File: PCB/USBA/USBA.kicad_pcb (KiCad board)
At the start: 2 copper layers, 70 x 70 mm, 23 parts, among them J1 USB_A, J2 Shelly, U2 ESP32-S3-MINI-1, U5 MD8942, U6 SHT40

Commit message: New reg
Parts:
- moved R10 1.30 mm to (104.8, 102.0), turned to 180 degrees
- moved R11 1.30 mm to (108.4, 102.0), turned to 180 degrees
- moved R1 0.30 mm to (108.7, 104.4)
- moved C3 0.30 mm to (108.7, 103.5)
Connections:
- U2 pad 21: unconnected-(U2-GPIO17-Pad21) -> GND
- U2 pad 22: unconnected-(U2-GPIO18-Pad22) -> GND
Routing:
- net GND: track 7.65 -> 7.76 mm, vias 15 -> 16

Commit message: Tidy
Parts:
- moved R4 0.10 mm to (104.8, 103.8)
- moved R5 0.10 mm to (104.8, 104.7)
- moved R7 0.10 mm to (104.8, 102.9)
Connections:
- U2 pad 21: GND -> unconnected-(U2-GPIO17-Pad21)
- U2 pad 22: GND -> unconnected-(U2-GPIO18-Pad22)
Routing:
- net GND: vias 16 -> 19

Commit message: Tweak
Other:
- board text added: "This PCB must be 1.2mm thick Please query if ordered otherwise"
- board text added: "This PCB must be 70x70mm Please query if ordered otherwise"
- board text removed: "Use 1.2mm PCB"

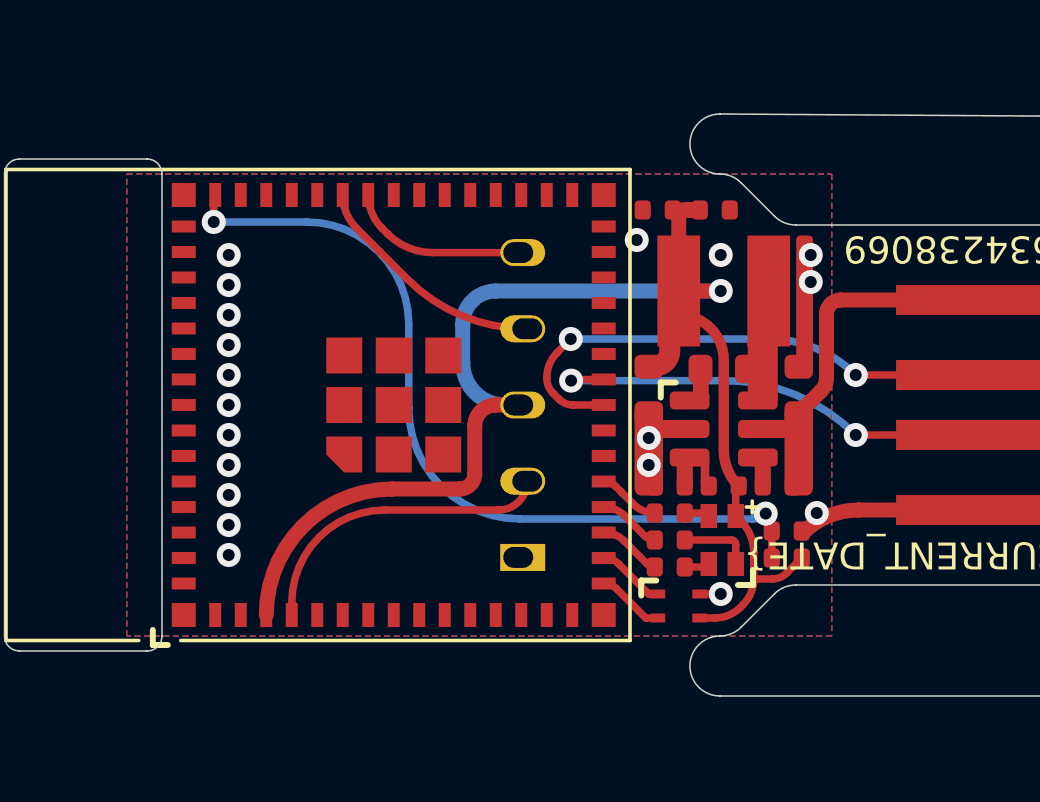
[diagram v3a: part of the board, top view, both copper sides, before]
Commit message: Added USB pads to allow programming in panel
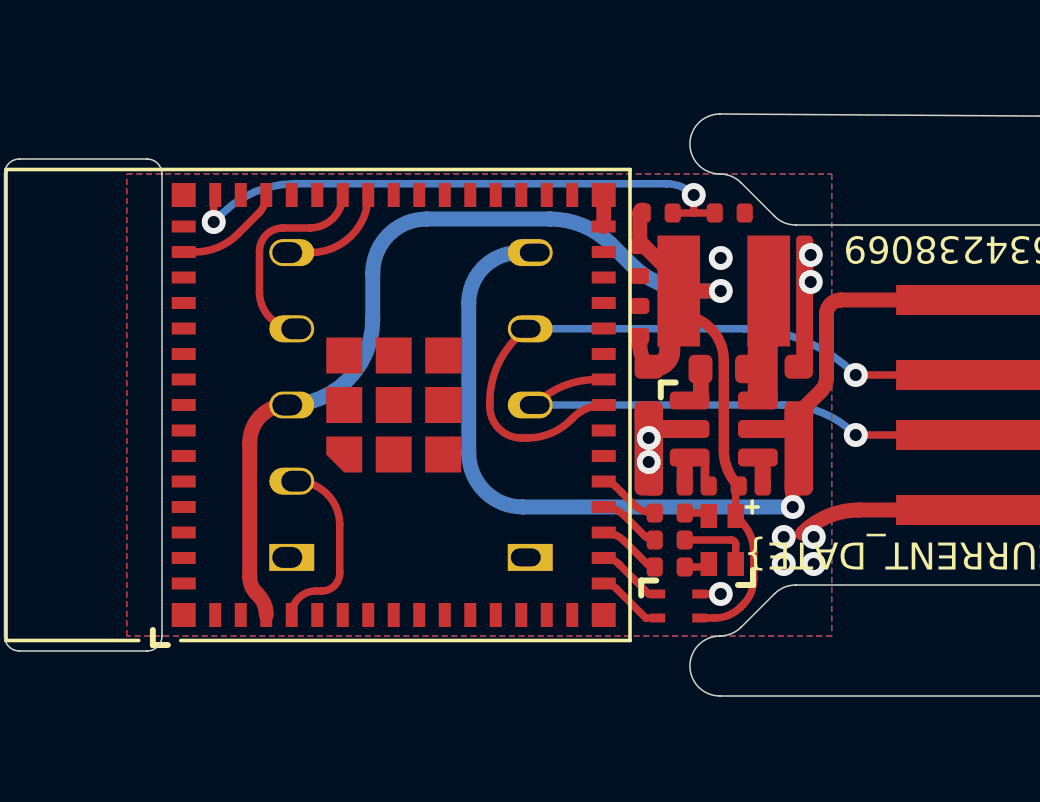
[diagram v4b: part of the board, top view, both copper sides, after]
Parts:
- added J3: USB-PROG, RevK:USB-PROG, B.Cu at (100.2, 99.3)
- moved R1 12.3 mm to (104.4, 92.9), turned to 0 degrees
- moved C3 10.8 mm to (106.8, 92.9)
- moved J2 7.70 mm to (92.2, 99.3)
- moved C1 3.75 mm to (103.8, 96.5), turned to 90 degrees
- moved C2 3.02 mm to (103.8, 94.5), turned to -90 degrees
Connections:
- U2 pad 21: unconnected-(U2-GPIO17-Pad21) -> GND
- U2 pad 22: unconnected-(U2-GPIO18-Pad22) -> GND
- U2 pad 27: unconnected-(U2-GPIO47-Pad27) -> GND
- U2 pad 28: unconnected-(U2-GPIO33-Pad28) -> GND
- U2 pad 29: unconnected-(U2-GPIO34-Pad29) -> GND
- U2 pad 30: unconnected-(U2-GPIO48-Pad30) -> GND
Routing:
- net VBUS: track 9.93 -> 31.8 mm, vias 0 -> 1
- net Net-(U2-EN): track 27.5 -> 19.3 mm
- net D-: track 18.3 -> 23.5 mm, vias 2 -> 1
- net GND: track 7.76 -> 12.4 mm, vias 19 -> 10
- net Net-(J2-0): track 10.4 -> 6.17 mm
- net D+: track 15.6 -> 18.0 mm, vias 2 -> 1
- net Net-(J2-Tx): track 6.00 -> 3.72 mm
- net Net-(J2-Rx): track 8.03 -> 7.01 mm
- net +3.3V: track 39.2 -> 38.6 mm
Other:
- board text removed: "Made in China for Andrews&Arnold Ltd"

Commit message: Tidy
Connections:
- U2 pad 44: unconnected-(U2-GPIO46-Pad44) -> GND
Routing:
- net GND: track 12.4 -> 8.77 mm, vias 10 -> 22

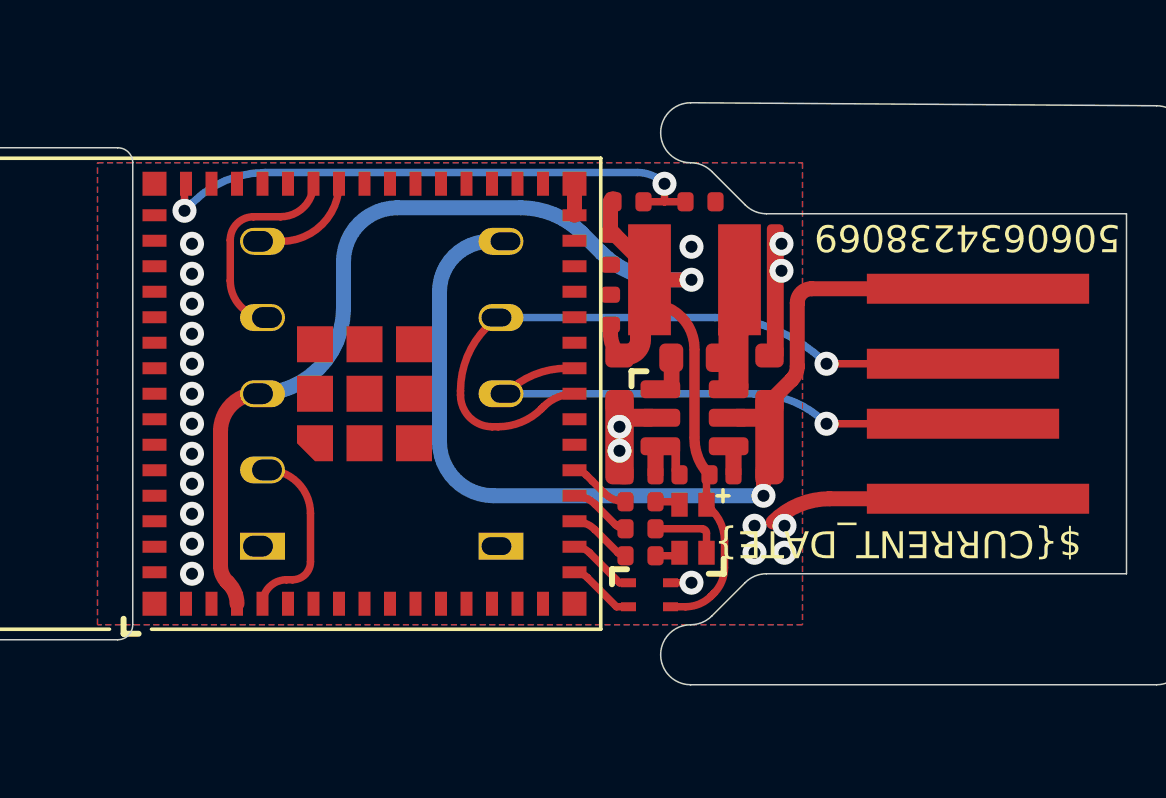
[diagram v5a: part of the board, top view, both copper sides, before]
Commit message: Changed to WS2812
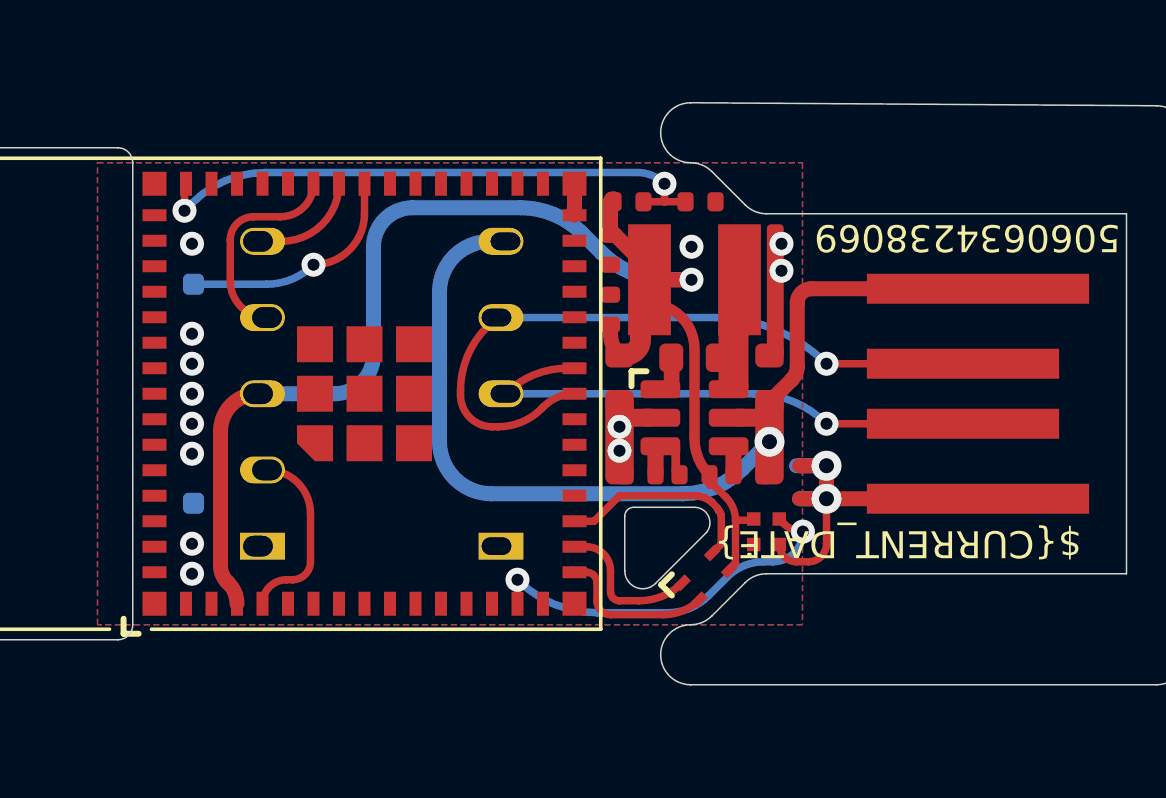
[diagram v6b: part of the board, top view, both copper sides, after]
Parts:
- removed D2: RGB, RevK:LED-RGB-1.6x1.6
- removed R4: 680R, RevK:R_0402
- removed R5: 2K, RevK:R_0402
- removed R7: 220R, RevK:R_0402
- added D1: XL-1010RGBC-WS2812B, RevK:SMD1010, F.Cu at (109.0, 103.9)
- added SW1: SW_Push, RevK:TS-1092S-B3D2-G, B.Cu at (89.9, 99.3)
- moved U6 1.98 mm to (107.0, 105.4), turned to 45 degrees
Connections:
- U2 pad 14: unconnected-(U2-GPIO10-Pad14) -> Net-(D1-I)
- U2 pad 18: G -> GND
- U2 pad 19: R -> unconnected-(U2-GPIO15-Pad19)
- U2 pad 20: B -> GND
- U2 pad 38: unconnected-(U2-GPIO42-Pad38) -> Net-(U2-GPIO42)
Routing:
- net GND: track 8.77 -> 21.5 mm, vias 22 -> 15
- net Net-(D1-I): track 0.00 -> 12.6 mm, vias 0 -> 2
- net Net-(U2-GPIO42): track 0.00 -> 7.76 mm, vias 0 -> 1
- net SCL: track 2.25 -> 5.33 mm
- net SDA: track 2.26 -> 5.03 mm
- net Net-(D2-RK): track 2.53 -> 0.00 mm
- net G: track 2.11 -> 0.00 mm
- net R: track 2.09 -> 0.00 mm
- net B: track 2.06 -> 0.00 mm
- net VBUS: track 31.8 -> 30.0 mm
- net +3.3V: track 38.6 -> 37.6 mm
- net Net-(D2-GK): track 0.80 -> 0.00 mm
- net Net-(D2-BK): track 0.80 -> 0.00 mm
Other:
- board text added: "WS2812:10 SCL:12 SDA:13"
- board text removed: "RGB: 15/14/16 SCL: 12 SDA: 13"

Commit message: Silk
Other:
- board text added: "WS2812:10 SCL:12 SDA:13 BTN:42"
- board text removed: "WS2812:10 SCL:12 SDA:13"

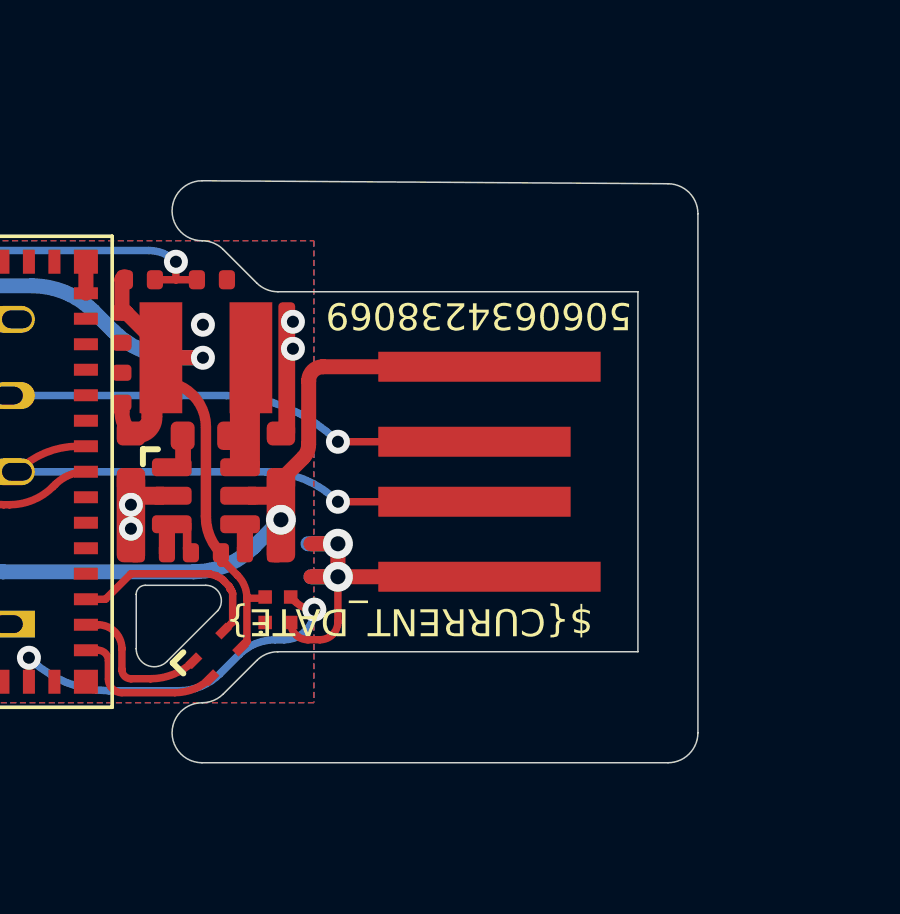
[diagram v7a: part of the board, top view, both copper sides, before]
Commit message: Slight angle fixed
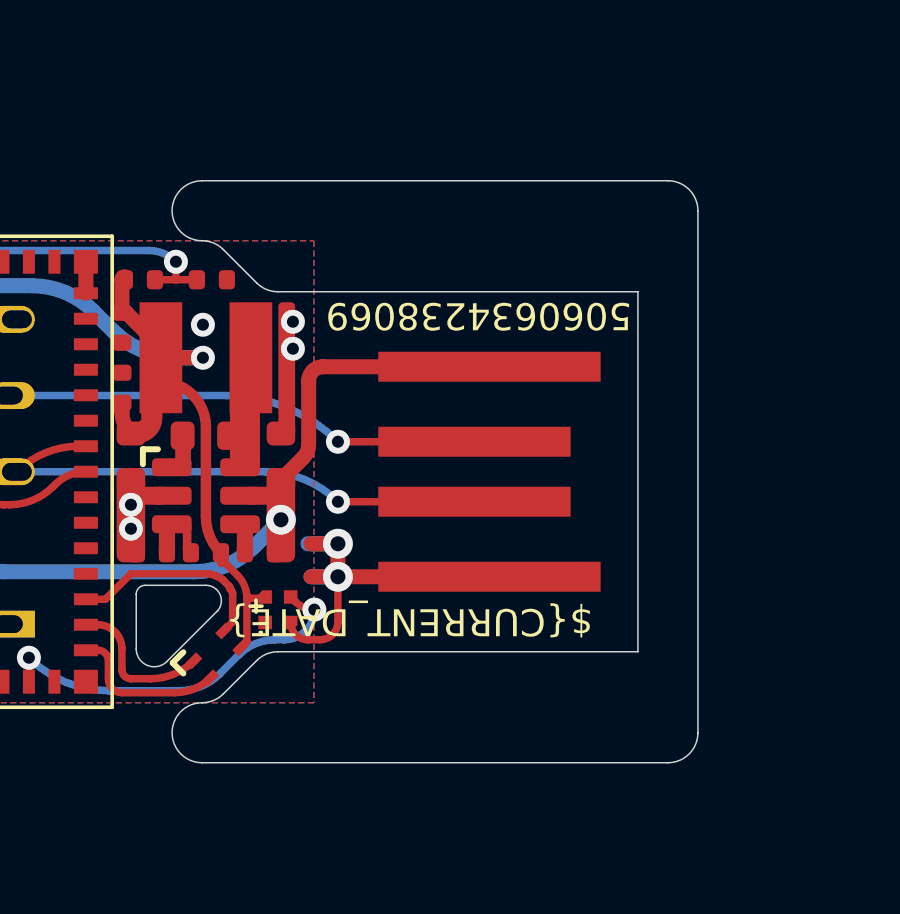
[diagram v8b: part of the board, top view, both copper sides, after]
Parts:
- V1, V2: footprint RevK:VCUT70 -> RevK:VCUT70N
